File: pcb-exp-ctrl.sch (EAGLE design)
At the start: 18 parts, among them IC1 SAA1064, IC2 TINY13-20PU, T1 BC547, T2 BC547

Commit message: spannungsregler nebst elko hinzugefügt
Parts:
- added C4: 2.2u, rcl:CPOL-EUE2.5-6
- added IC3: LP2950Z, national-semiconductor:LP2950Z
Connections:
- net +5V: now also C4.+, IC3.O
- net GND: now also C4.-, IC3.GND
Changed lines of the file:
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@@
 <part name="GND2" library="supply1" deviceset="GND" device=""/>
 <part name="P+1" library="supply1" deviceset="+5V" device=""/>
-<part name="P+2" library="supply1" deviceset="+5V" device=""/>
 <part name="SJ1" library="jumper" deviceset="SJ2W" device=""/>
 <part name="R1" library="rcl" deviceset="R-EU_" device="0204/7" value="10k"/>
@@
 <part name="S2" library="switch-misc" deviceset="SRKL" device=""/>
 <part name="S3" library="switch-misc" deviceset="SRKL" device=""/>
+<part name="IC3" library="national-semiconductor" deviceset="LP2950" device="Z"/>
+<part name="C4" library="rcl" deviceset="CPOL-EU" device="E2.5-6" value="2.2u"/>
 </parts>
 <sheets>
@@
 <instance part="GND1" gate="1" x="-30.48" y="-5.08"/>
 <instance part="GND2" gate="1" x="0" y="38.1"/>
-<instance part="P+1" gate="1" x="-7.62" y="104.14"/>
-<instance part="P+2" gate="1" x="-30.48" y="27.94"/>
+<instance part="P+1" gate="1" x="-30.48" y="106.68"/>
 <instance part="SJ1" gate="G$1" x="0" y="63.5" rot="R180"/>
 <instance part="R1" gate="G$1" x="-15.24" y="83.82" rot="R90"/>
@@
 <instance part="S3" gate="1" x="12.7" y="-30.48"/>
 <instance part="S3" gate="D1" x="20.32" y="-33.02"/>
+<instance part="IC3" gate="G$1" x="-71.12" y="93.98"/>
+<instance part="C4" gate="G$1" x="-50.8" y="91.44"/>
 </instances>
 <busses>
@@
 <junction x="-15.24" y="71.12"/>
 <pinref part="SV1" gate="1" pin="4"/>
-<wire x1="-60.96" y1="35.56" x2="-66.04" y2="35.56" width="0.1524" layer="91"/>
-<wire x1="-66.04" y1="35.56" x2="-66.04" y2="45.72" width="0.1524" layer="91"/>
-<wire x1="-66.04" y1="45.72" x2="-15.24" y2="45.72" width="0.1524" layer="91"/>
+<wire x1="-60.96" y1="35.56" x2="-63.5" y2="35.56" width="0.1524" layer="91"/>
+<wire x1="-63.5" y1="35.56" x2="-63.5" y2="45.72" width="0.1524" layer="91"/>
+<wire x1="-63.5" y1="45.72" x2="-15.24" y2="45.72" width="0.1524" layer="91"/>
 <junction x="-15.24" y="45.72"/>
 </segment>
@@
 <junction x="-30.48" y="2.54"/>
 <pinref part="SV1" gate="1" pin="6"/>
-<wire x1="-60.96" y1="38.1" x2="-63.5" y2="38.1" width="0.1524" layer="91"/>
-<wire x1="-63.5" y1="38.1" x2="-63.5" y2="2.54" width="0.1524" layer="91"/>
-<wire x1="-63.5" y1="2.54" x2="-30.48" y2="2.54" width="0.1524" layer="91"/>
+<wire x1="-60.96" y1="38.1" x2="-71.12" y2="38.1" width="0.1524" layer="91"/>
+<wire x1="-71.12" y1="38.1" x2="-71.12" y2="2.54" width="0.1524" layer="91"/>
+<wire x1="-71.12" y1="2.54" x2="-30.48" y2="2.54" width="0.1524" layer="91"/>
+<pinref part="IC3" gate="G$1" pin="GND"/>
+<wire x1="-71.12" y1="88.9" x2="-71.12" y2="83.82" width="0.1524" layer="91"/>
+<junction x="-71.12" y="38.1"/>
+<pinref part="C4" gate="G$1" pin="-"/>
+<wire x1="-71.12" y1="83.82" x2="-71.12" y2="38.1" width="0.1524" layer="91"/>
+<wire x1="-50.8" y1="86.36" x2="-50.8" y2="83.82" width="0.1524" layer="91"/>
+<wire x1="-50.8" y1="83.82" x2="-71.12" y2="83.82" width="0.1524" layer="91"/>
+<junction x="-71.12" y="83.82"/>
 </segment>
 <segment>
@@
 <wire x1="0" y1="43.18" x2="-7.62" y2="43.18" width="0.1524" layer="91"/>
 <wire x1="-7.62" y1="43.18" x2="-7.62" y2="45.72" width="0.1524" layer="91"/>
-</segment>
-</net>
-<net name="+5V" class="0">
-<segment>
-<pinref part="P+1" gate="1" pin="+5V"/>
-<wire x1="-7.62" y1="101.6" x2="-7.62" y2="99.06" width="0.1524" layer="91"/>
-<pinref part="T2" gate="G$1" pin="C"/>
-<wire x1="60.96" y1="93.98" x2="60.96" y2="99.06" width="0.1524" layer="91"/>
-<wire x1="60.96" y1="99.06" x2="53.34" y2="99.06" width="0.1524" layer="91"/>
-<pinref part="T1" gate="G$1" pin="C"/>
-<wire x1="53.34" y1="99.06" x2="0" y2="99.06" width="0.1524" layer="91"/>
-<wire x1="0" y1="99.06" x2="-7.62" y2="99.06" width="0.1524" layer="91"/>
-<wire x1="53.34" y1="45.72" x2="53.34" y2="99.06" width="0.1524" layer="91"/>
-<junction x="53.34" y="99.06"/>
-<junction x="-7.62" y="99.06"/>
-<pinref part="C2" gate="G$1" pin="1"/>
-<wire x1="-7.62" y1="53.34" x2="-7.62" y2="99.06" width="0.1524" layer="91"/>
-<pinref part="R2" gate="G$1" pin="2"/>
-<pinref part="R1" gate="G$1" pin="2"/>
-<wire x1="-15.24" y1="88.9" x2="-15.24" y2="99.06" width="0.1524" layer="91"/>
-<wire x1="-15.24" y1="99.06" x2="-22.86" y2="99.06" width="0.1524" layer="91"/>
-<wire x1="-22.86" y1="99.06" x2="-22.86" y2="88.9" width="0.1524" layer="91"/>
-<wire x1="-7.62" y1="99.06" x2="-15.24" y2="99.06" width="0.1524" layer="91"/>
-<pinref part="IC1" gate="G$1" pin="VCC"/>
-<wire x1="0" y1="86.36" x2="10.16" y2="86.36" width="0.1524" layer="91"/>
-<pinref part="SJ1" gate="G$1" pin="3"/>
-<wire x1="0" y1="68.58" x2="0" y2="86.36" width="0.1524" layer="91"/>
-<wire x1="0" y1="86.36" x2="0" y2="99.06" width="0.1524" layer="91"/>
-<junction x="-15.24" y="99.06"/>
-<junction x="0" y="99.06"/>
-<junction x="0" y="86.36"/>
-<pinref part="SV1" gate="1" pin="2"/>
-<wire x1="-60.96" y1="33.02" x2="-68.58" y2="33.02" width="0.1524" layer="91"/>
-<wire x1="-68.58" y1="33.02" x2="-68.58" y2="99.06" width="0.1524" layer="91"/>
-<wire x1="-68.58" y1="99.06" x2="-22.86" y2="99.06" width="0.1524" layer="91"/>
-<junction x="-22.86" y="99.06"/>
-</segment>
-<segment>
-<pinref part="P+2" gate="1" pin="+5V"/>
-<pinref part="IC2" gate="G$1" pin="VCC"/>
-<wire x1="-30.48" y1="25.4" x2="-30.48" y2="20.32" width="0.1524" layer="91"/>
-<wire x1="-30.48" y1="20.32" x2="-38.1" y2="20.32" width="0.1524" layer="91"/>
-<pinref part="C3" gate="G$1" pin="1"/>
-<wire x1="-30.48" y1="20.32" x2="-2.54" y2="20.32" width="0.1524" layer="91"/>
-<wire x1="-30.48" y1="15.24" x2="-30.48" y2="20.32" width="0.1524" layer="91"/>
-<junction x="-30.48" y="20.32"/>
-<pinref part="R3" gate="G$1" pin="2"/>
-<wire x1="-38.1" y1="17.78" x2="-38.1" y2="20.32" width="0.1524" layer="91"/>
 </segment>
 </net>
@@
 </segment>
 </net>
+<net name="+5V" class="0">
+<segment>
+<pinref part="T2" gate="G$1" pin="C"/>
+<wire x1="60.96" y1="93.98" x2="60.96" y2="99.06" width="0.1524" layer="91"/>
+<wire x1="60.96" y1="99.06" x2="53.34" y2="99.06" width="0.1524" layer="91"/>
+<pinref part="T1" gate="G$1" pin="C"/>
+<wire x1="53.34" y1="99.06" x2="0" y2="99.06" width="0.1524" layer="91"/>
+<wire x1="0" y1="99.06" x2="-7.62" y2="99.06" width="0.1524" layer="91"/>
+<wire x1="53.34" y1="45.72" x2="53.34" y2="99.06" width="0.1524" layer="91"/>
+<junction x="53.34" y="99.06"/>
+<junction x="-7.62" y="99.06"/>
+<pinref part="C2" gate="G$1" pin="1"/>
+<wire x1="-7.62" y1="53.34" x2="-7.62" y2="99.06" width="0.1524" layer="91"/>
+<pinref part="R2" gate="G$1" pin="2"/>
+<pinref part="R1" gate="G$1" pin="2"/>
+<wire x1="-15.24" y1="88.9" x2="-15.24" y2="99.06" width="0.1524" layer="91"/>
+<wire x1="-15.24" y1="99.06" x2="-22.86" y2="99.06" width="0.1524" layer="91"/>
+<wire x1="-22.86" y1="99.06" x2="-22.86" y2="88.9" width="0.1524" layer="91"/>
+<wire x1="-7.62" y1="99.06" x2="-15.24" y2="99.06" width="0.1524" layer="91"/>
+<pinref part="IC1" gate="G$1" pin="VCC"/>
+<wire x1="0" y1="86.36" x2="10.16" y2="86.36" width="0.1524" layer="91"/>
+<pinref part="SJ1" gate="G$1" pin="3"/>
+<wire x1="0" y1="68.58" x2="0" y2="86.36" width="0.1524" layer="91"/>
+<wire x1="0" y1="86.36" x2="0" y2="99.06" width="0.1524" layer="91"/>
+<junction x="-15.24" y="99.06"/>
+<junction x="0" y="99.06"/>
+<junction x="0" y="86.36"/>
+<pinref part="SV1" gate="1" pin="2"/>
+<wire x1="-60.96" y1="33.02" x2="-66.04" y2="33.02" width="0.1524" layer="91"/>
+<wire x1="-66.04" y1="33.02" x2="-66.04" y2="48.26" width="0.1524" layer="91"/>
+<wire x1="-66.04" y1="48.26" x2="-30.48" y2="48.26" width="0.1524" layer="91"/>
+<wire x1="-30.48" y1="48.26" x2="-30.48" y2="99.06" width="0.1524" layer="91"/>
+<wire x1="-30.48" y1="99.06" x2="-22.86" y2="99.06" width="0.1524" layer="91"/>
+<junction x="-22.86" y="99.06"/>
+<pinref part="IC3" gate="G$1" pin="O"/>
+<wire x1="-60.96" y1="99.06" x2="-50.8" y2="99.06" width="0.1524" layer="91"/>
+<junction x="-30.48" y="99.06"/>
+<pinref part="IC2" gate="G$1" pin="VCC"/>
+<wire x1="-50.8" y1="99.06" x2="-30.48" y2="99.06" width="0.1524" layer="91"/>
+<wire x1="-30.48" y1="20.32" x2="-38.1" y2="20.32" width="0.1524" layer="91"/>
+<pinref part="C3" gate="G$1" pin="1"/>
+<wire x1="-30.48" y1="20.32" x2="-2.54" y2="20.32" width="0.1524" layer="91"/>
+<wire x1="-30.48" y1="15.24" x2="-30.48" y2="20.32" width="0.1524" layer="91"/>
+<junction x="-30.48" y="20.32"/>
+<pinref part="R3" gate="G$1" pin="2"/>
+<wire x1="-38.1" y1="17.78" x2="-38.1" y2="20.32" width="0.1524" layer="91"/>
+<wire x1="-30.48" y1="20.32" x2="-30.48" y2="48.26" width="0.1524" layer="91"/>
+<junction x="-30.48" y="48.26"/>
+<pinref part="P+1" gate="1" pin="+5V"/>
+<wire x1="-30.48" y1="104.14" x2="-30.48" y2="99.06" width="0.1524" layer="91"/>
+<pinref part="C4" gate="G$1" pin="+"/>
+<wire x1="-50.8" y1="93.98" x2="-50.8" y2="99.06" width="0.1524" layer="91"/>
+<junction x="-50.8" y="99.06"/>
+</segment>
+</net>

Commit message: add NPN for switching UV LEDs
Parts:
- added T3: BD131, transistor:-NPN-TO126V
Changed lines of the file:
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@@
 <part name="IC3" library="national-semiconductor" deviceset="LP2950" device="Z"/>
 <part name="C4" library="rcl" deviceset="CPOL-EU" device="E2.5-6" value="2.2u"/>
+<part name="T3" library="transistor" deviceset="*-NPN-" device="TO126V" value="BD131"/>
 </parts>
 <sheets>
@@
 <instance part="IC3" gate="G$1" x="-71.12" y="93.98"/>
 <instance part="C4" gate="G$1" x="-50.8" y="91.44"/>
+<instance part="T3" gate="G$1" x="73.66" y="-25.4"/>
 </instances>
 <busses>

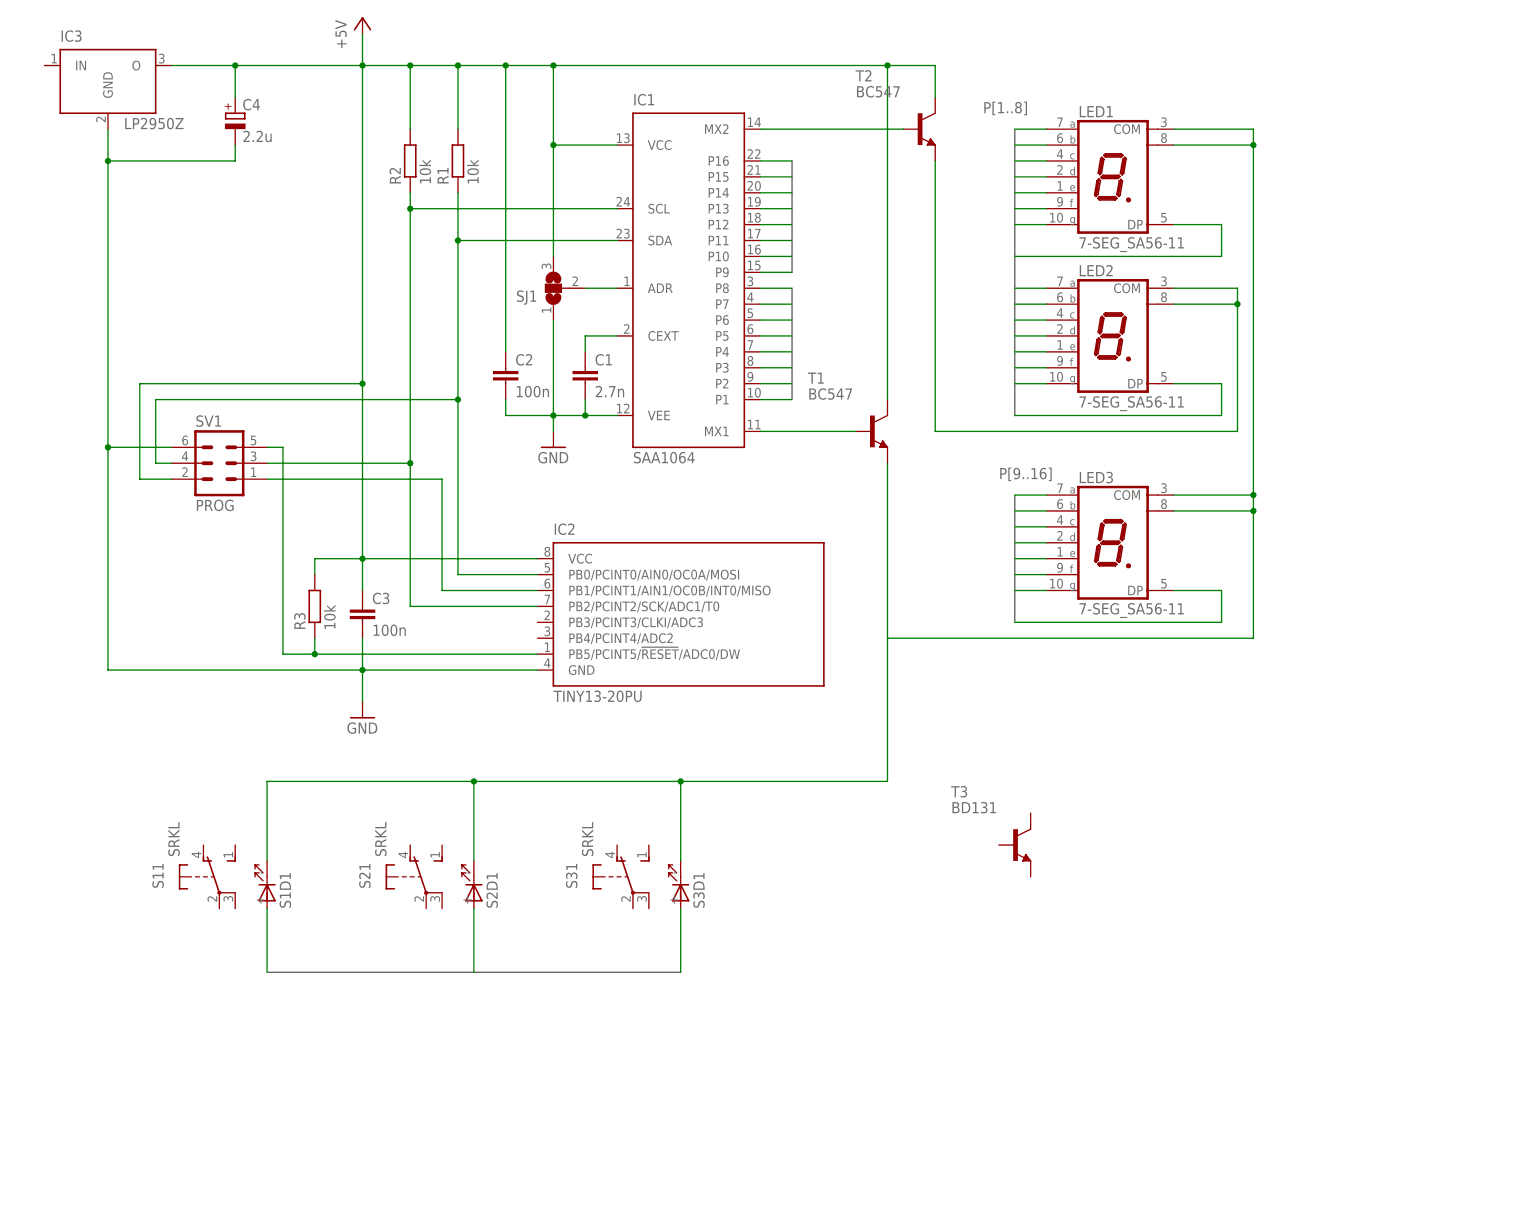
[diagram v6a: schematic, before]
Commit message: replace NPN with relay
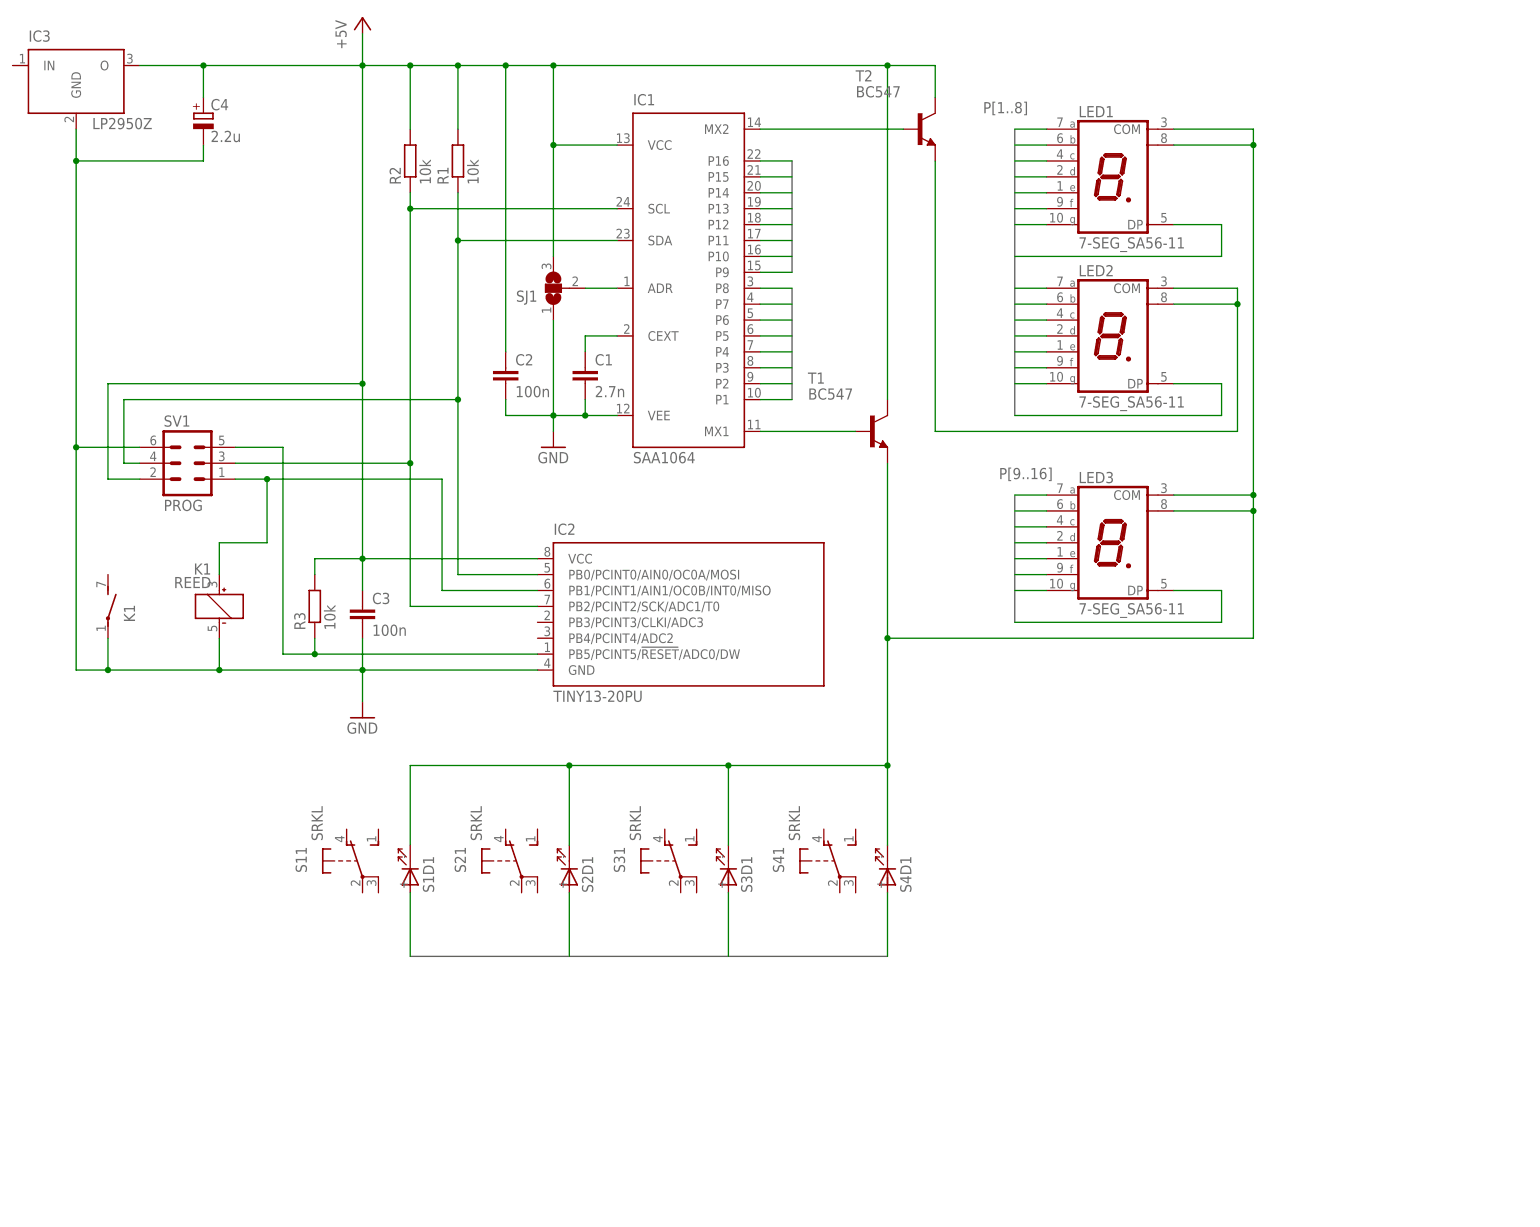
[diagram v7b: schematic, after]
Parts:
- removed T3: BD131, transistor:-NPN-TO126V
- added K1: REED, relay:REED
- added S4: SRKL, switch-misc:SRKL
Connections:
- net GND: now also K11.-, K12.P
- net MISO: now also K11.+
- net N$7: now also S4D1.C
- net P12: now also S4D1.A
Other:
- moved on the sheet: C4, IC3, S11, S1D1, S21, S2D1, S31, S3D1, SV1

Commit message: extra LEDs korrekt verdrahtet
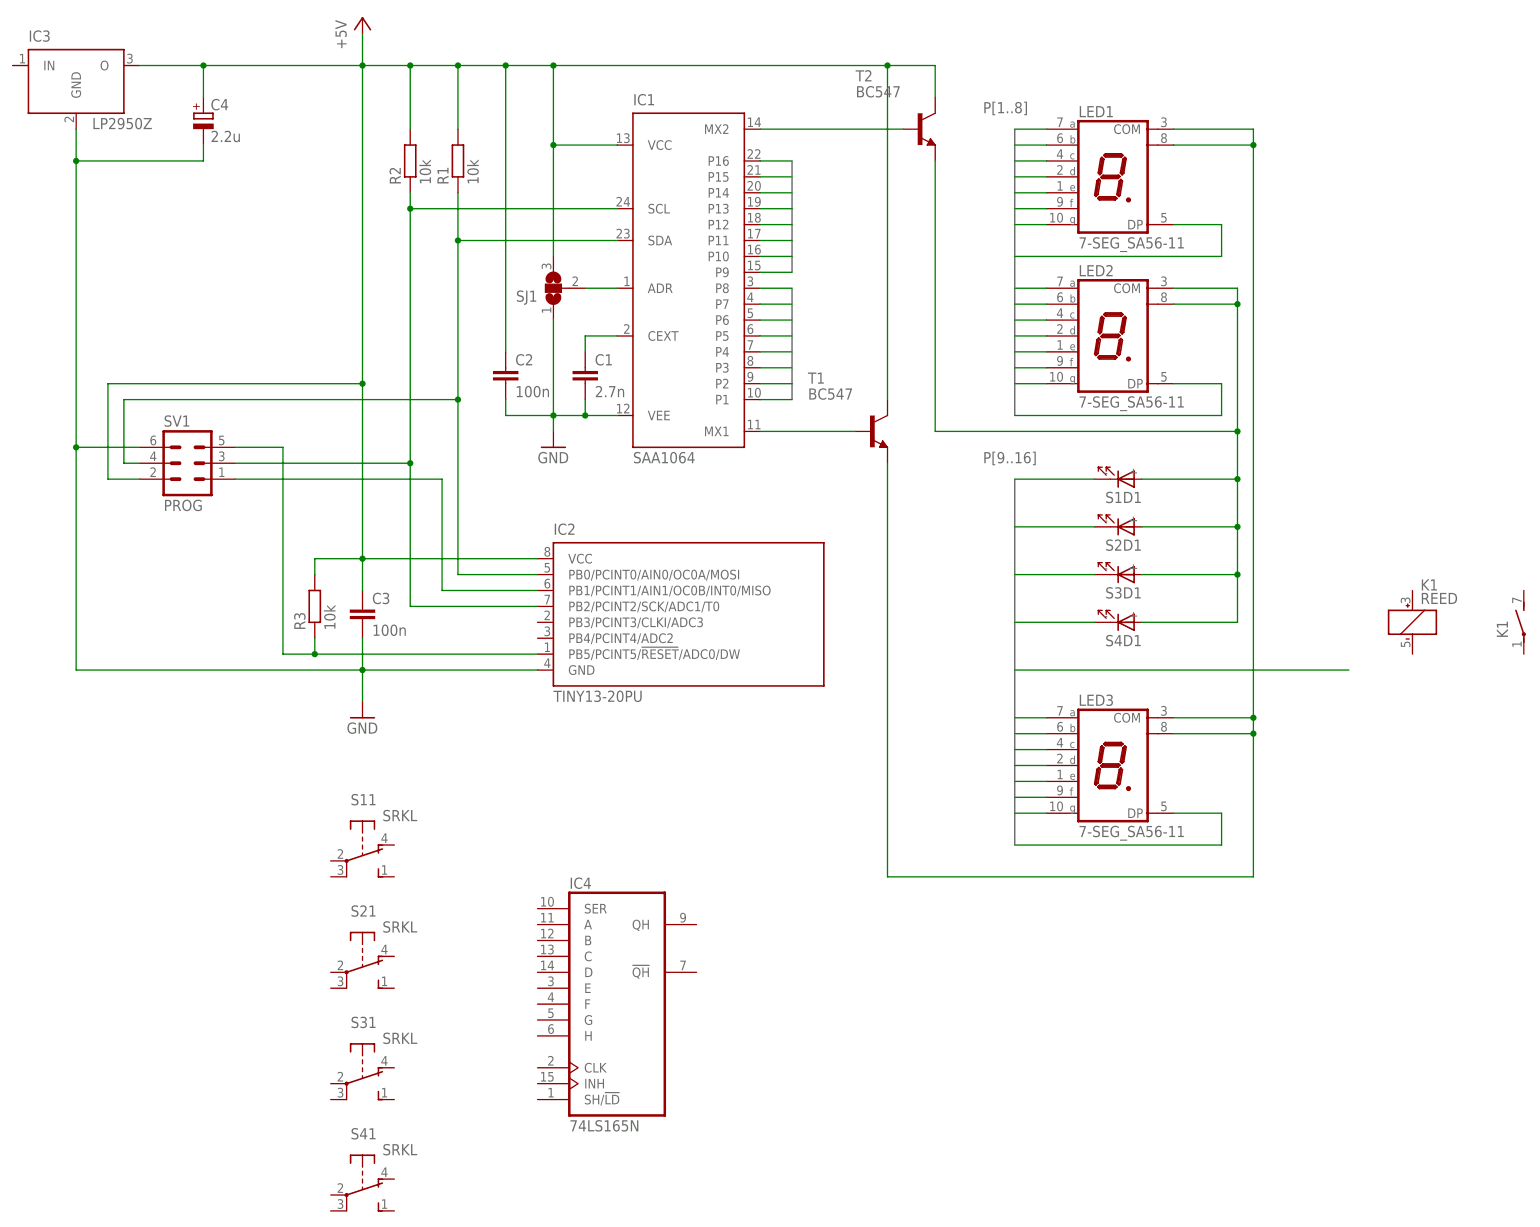
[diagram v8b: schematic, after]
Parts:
- added IC4: 74LS165N, 74xx-eu:74LS165N
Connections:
- net GND: no longer K11.-, K12.P
- net MISO: no longer K11.+
- net N$2: now also S1D1.A, S2D1.A, S3D1.A, S4D1.A
- net N$7: no longer S1D1.C, S2D1.C, S3D1.C, S4D1.C
- net P10: now also S2D1.C; no longer S2D1.A
- net P11: now also S3D1.C; no longer S3D1.A
- net P12: now also S4D1.C; no longer S4D1.A
- net P9: now also S1D1.C; no longer S1D1.A
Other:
- moved on the sheet: K1, LED3, S11, S1D1, S21, S2D1, S31, S3D1, S41, S4D1
